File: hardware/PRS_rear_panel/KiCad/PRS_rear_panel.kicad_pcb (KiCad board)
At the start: 2 copper layers, 203 x 51 mm, 0 parts

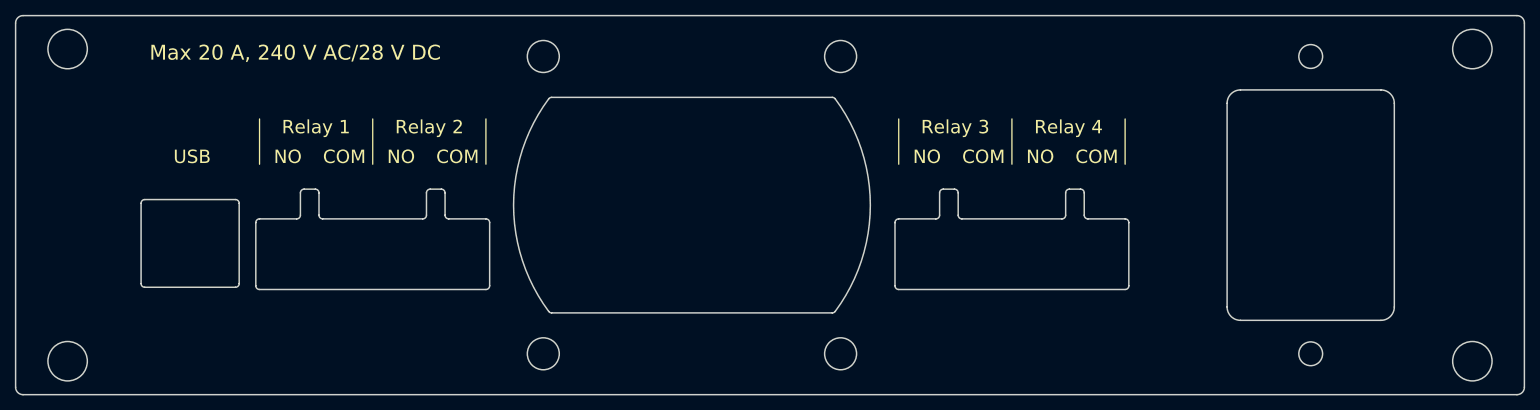
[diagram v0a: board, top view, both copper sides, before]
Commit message: Update PRS_rear_panel to KiCad v6
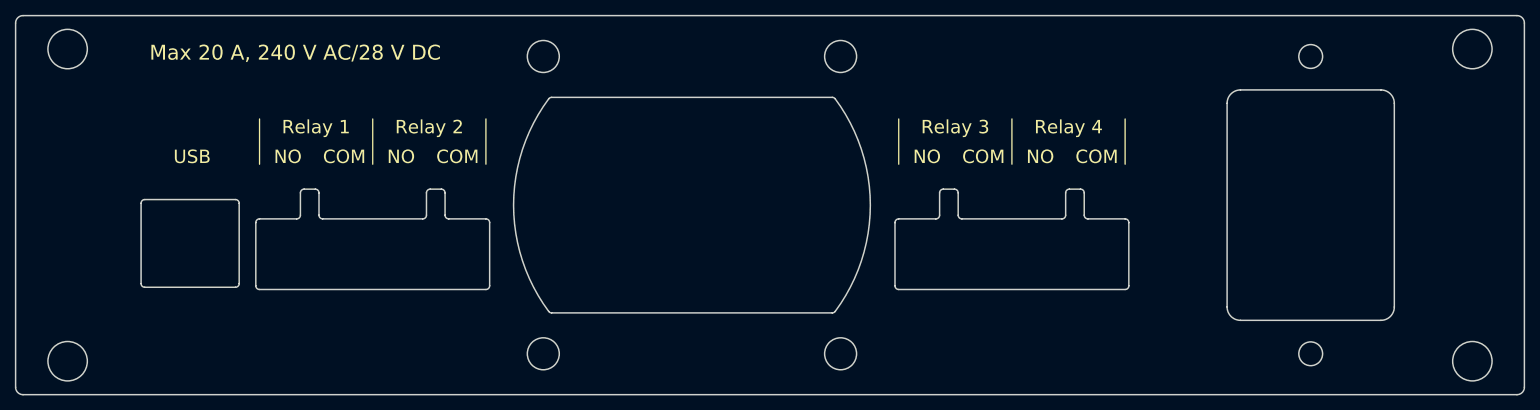
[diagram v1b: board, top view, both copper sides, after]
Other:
- net class Default removed
